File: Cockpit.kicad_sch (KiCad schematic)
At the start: 49 parts, among them J2 PI_GPIO_40, J3 CAN_A_PROBE, J4 CAN_B_PROBE, SW1 219-2MSTR, SW2 CVS-01TB, SW3 219-2MSTR, SW4 CVS-01TB, U4 MCP2515T-I/ST, U5 SN65HVD230DR, U6 MCP2515T-I/ST, U6 SN65HVD230DR, Y1 16 MHz, Y2 16 MHz

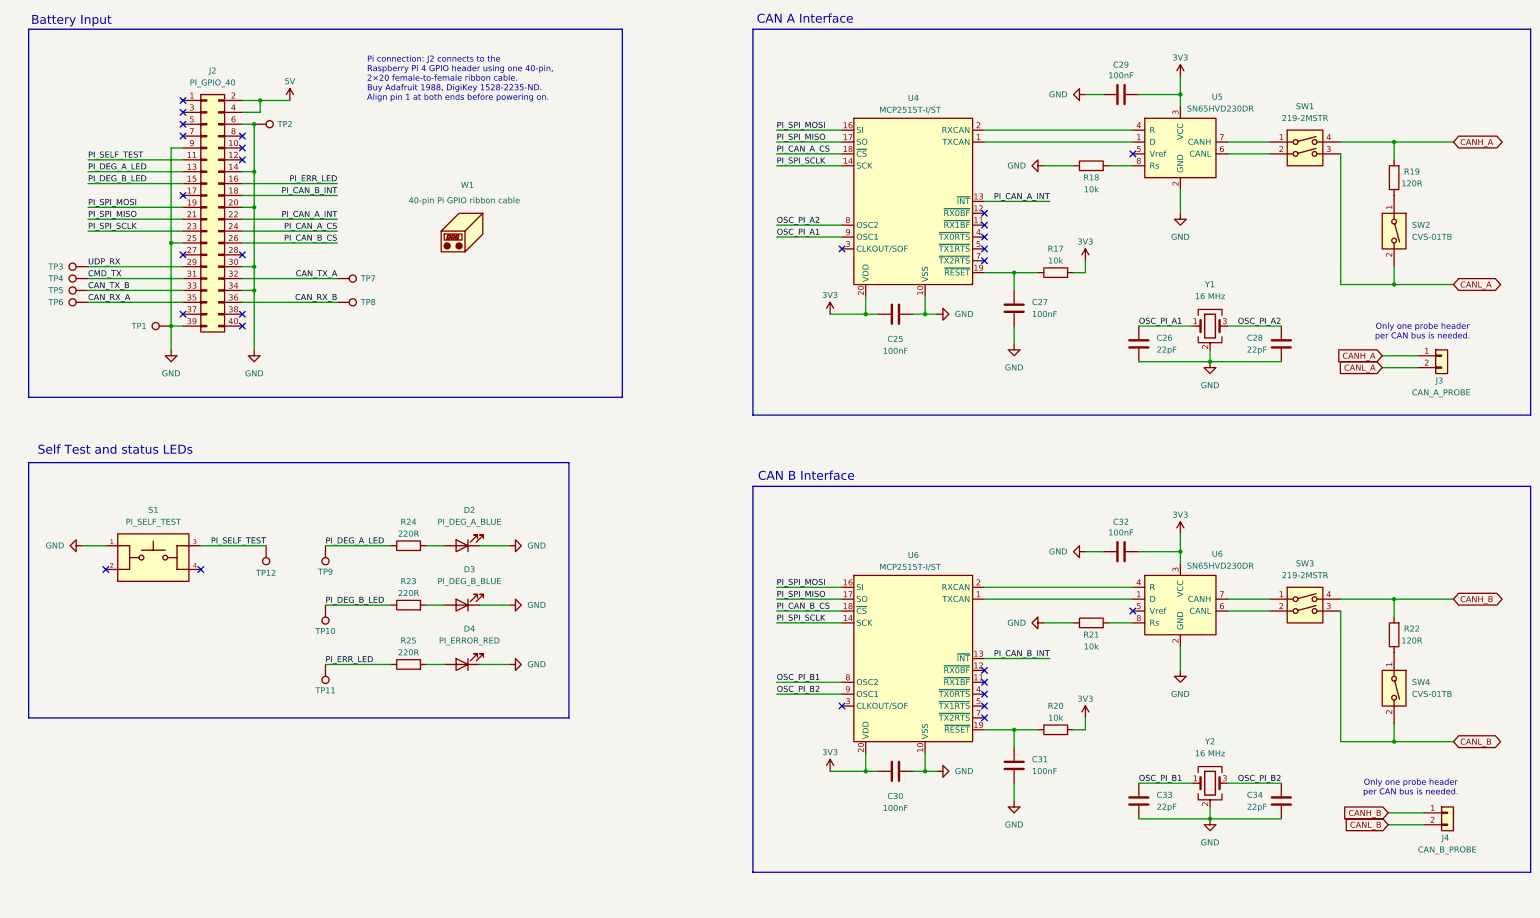
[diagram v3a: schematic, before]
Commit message: Re-annotate whole schematic (sheet x100); drivetrain SCLK fix, BOM fields, footprints
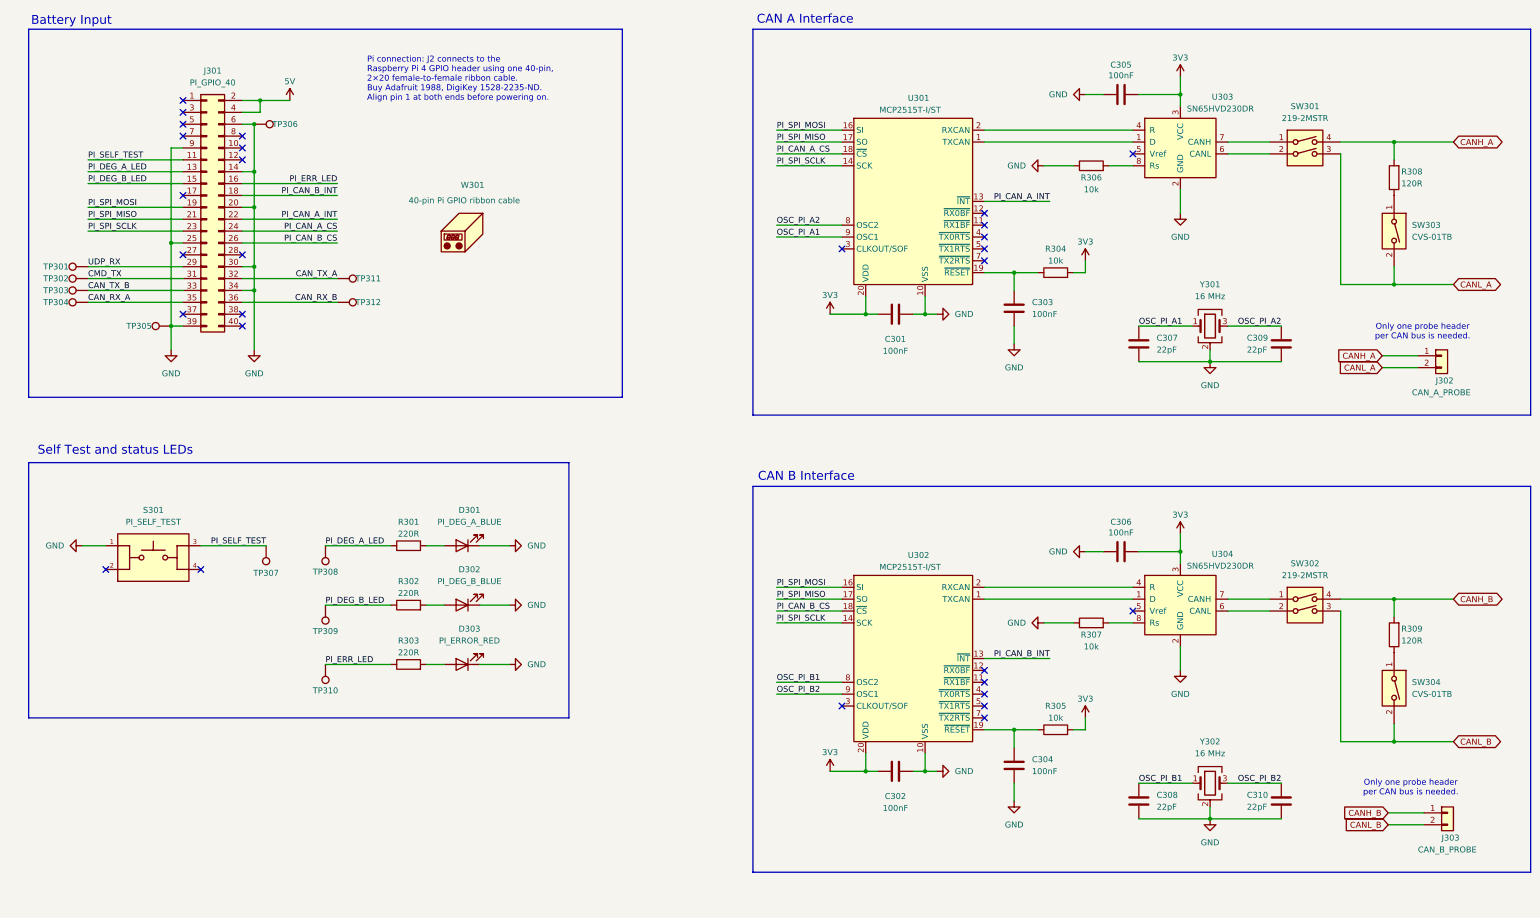
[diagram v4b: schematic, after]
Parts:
- renumbered C25 to C301, C30 to C302, C27 to C303, C31 to C304, C29 to C305, C32 to C306, C26 to C307, C33 to C308, C28 to C309, C34 to C310, D2 to D301, D3 to D302, D4 to D303, J2 to J301, J3 to J302, J4 to J303, R24 to R301, R23 to R302, R25 to R303, R17 to R304, R20 to R305, R18 to R306, R21 to R307, R19 to R308, R22 to R309, S1 to S301, SW1 to SW301, SW3 to SW302, SW2 to SW303, SW4 to SW304, TP3 to TP301, TP4 to TP302, TP5 to TP303, TP6 to TP304, TP1 to TP305, TP2 to TP306, TP12 to TP307, TP9 to TP308, TP10 to TP309, TP11 to TP310, TP7 to TP311, TP8 to TP312, U4 to U301, U6 to U302, U5 to U303, U6 to U304, W1 to W301, Y1 to Y301, Y2 to Y302

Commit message: DT layout done
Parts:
- added H1, H2, H3, H4: MountingHole, MountingHole:MountingHole_3.2mm_M3, symbol Mechanical:MountingHole
